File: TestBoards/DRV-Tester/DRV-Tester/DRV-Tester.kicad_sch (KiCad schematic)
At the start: 0 parts

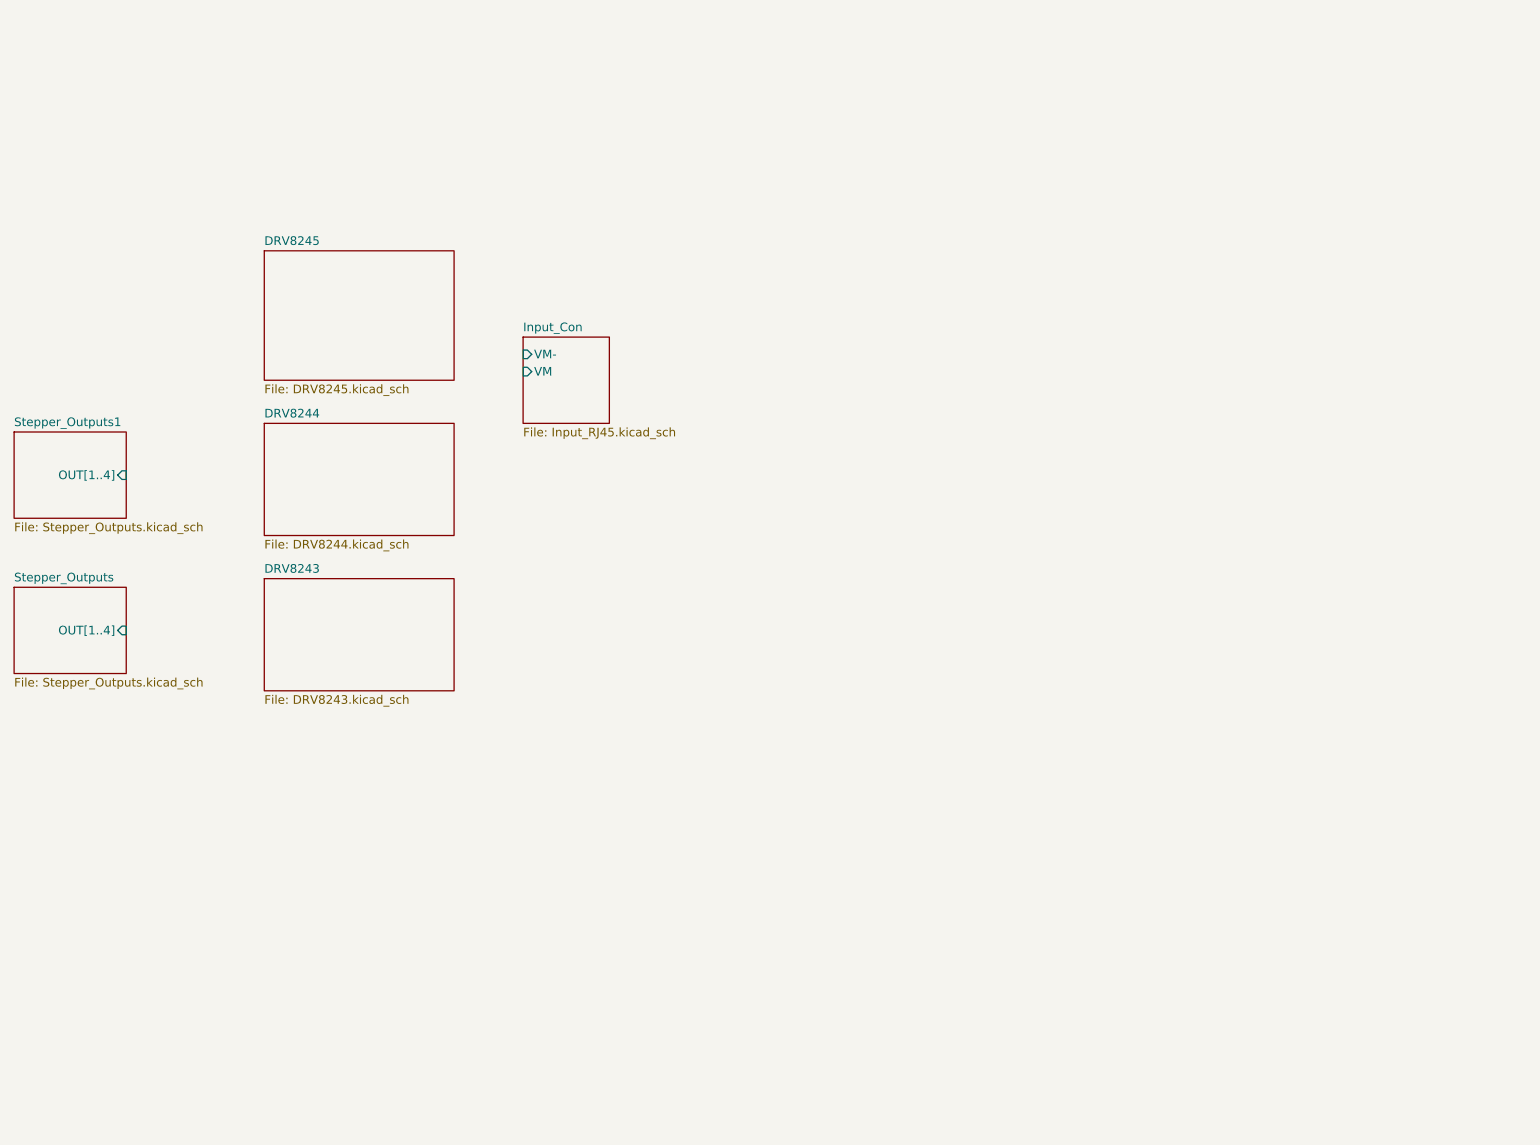
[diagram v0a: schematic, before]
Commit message: update new tester board sch
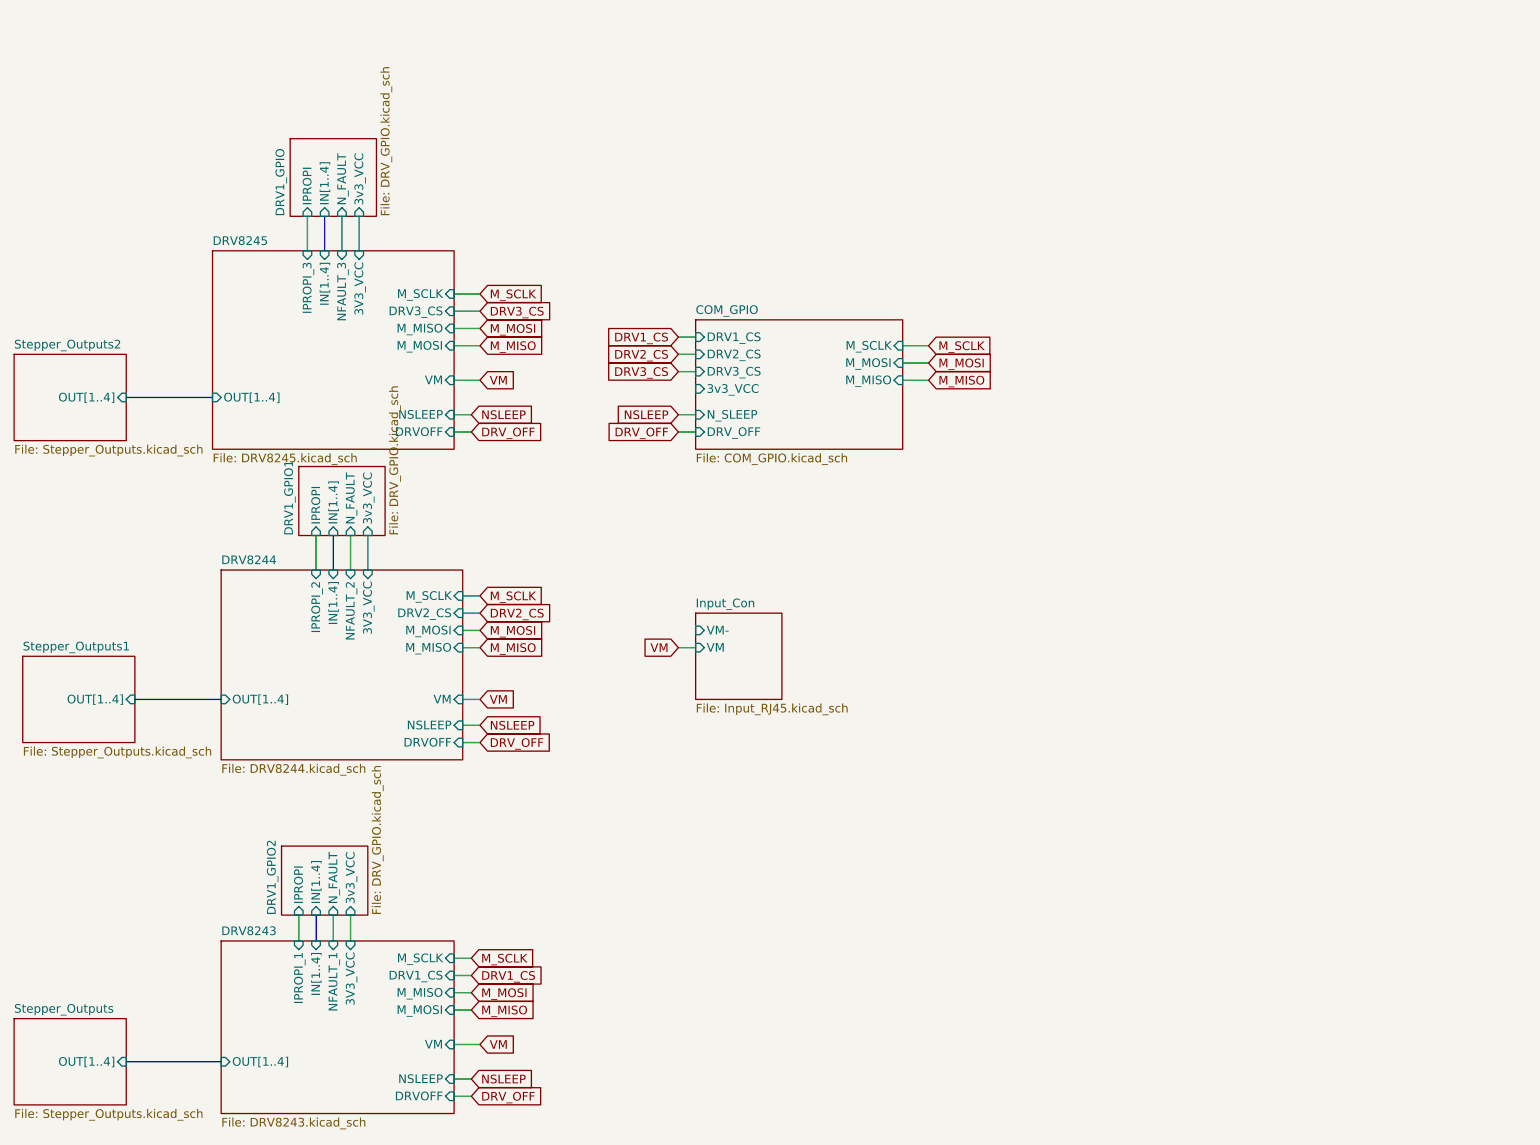
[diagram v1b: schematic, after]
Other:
- added sheet COM_GPIO (COM_GPIO.kicad_sch)
- added sheet DRV1_GPIO (DRV_GPIO.kicad_sch)
- added sheet DRV1_GPIO1 (DRV_GPIO.kicad_sch)
- added sheet DRV1_GPIO2 (DRV_GPIO.kicad_sch)
- added sheet Stepper_Outputs2 (Stepper_Outputs.kicad_sch)
- sheet DRV8243 ports: added 3V3_VCC, DRV1_CS, DRVOFF, IN[1..4], IPROPI_1, M_MISO, M_MOSI, M_SCLK, NFAULT_1, NSLEEP, OUT[1..4], VM; removed none
- sheet DRV8244 ports: added 3V3_VCC, DRV2_CS, DRVOFF, IN[1..4], IPROPI_2, M_MISO, M_MOSI, M_SCLK, NFAULT_2, NSLEEP, OUT[1..4], VM; removed none
- sheet DRV8245 ports: added 3V3_VCC, DRV3_CS, DRVOFF, IN[1..4], IPROPI_3, M_MISO, M_MOSI, M_SCLK, NFAULT_3, NSLEEP, OUT[1..4], VM; removed none

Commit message: update tester board with layout
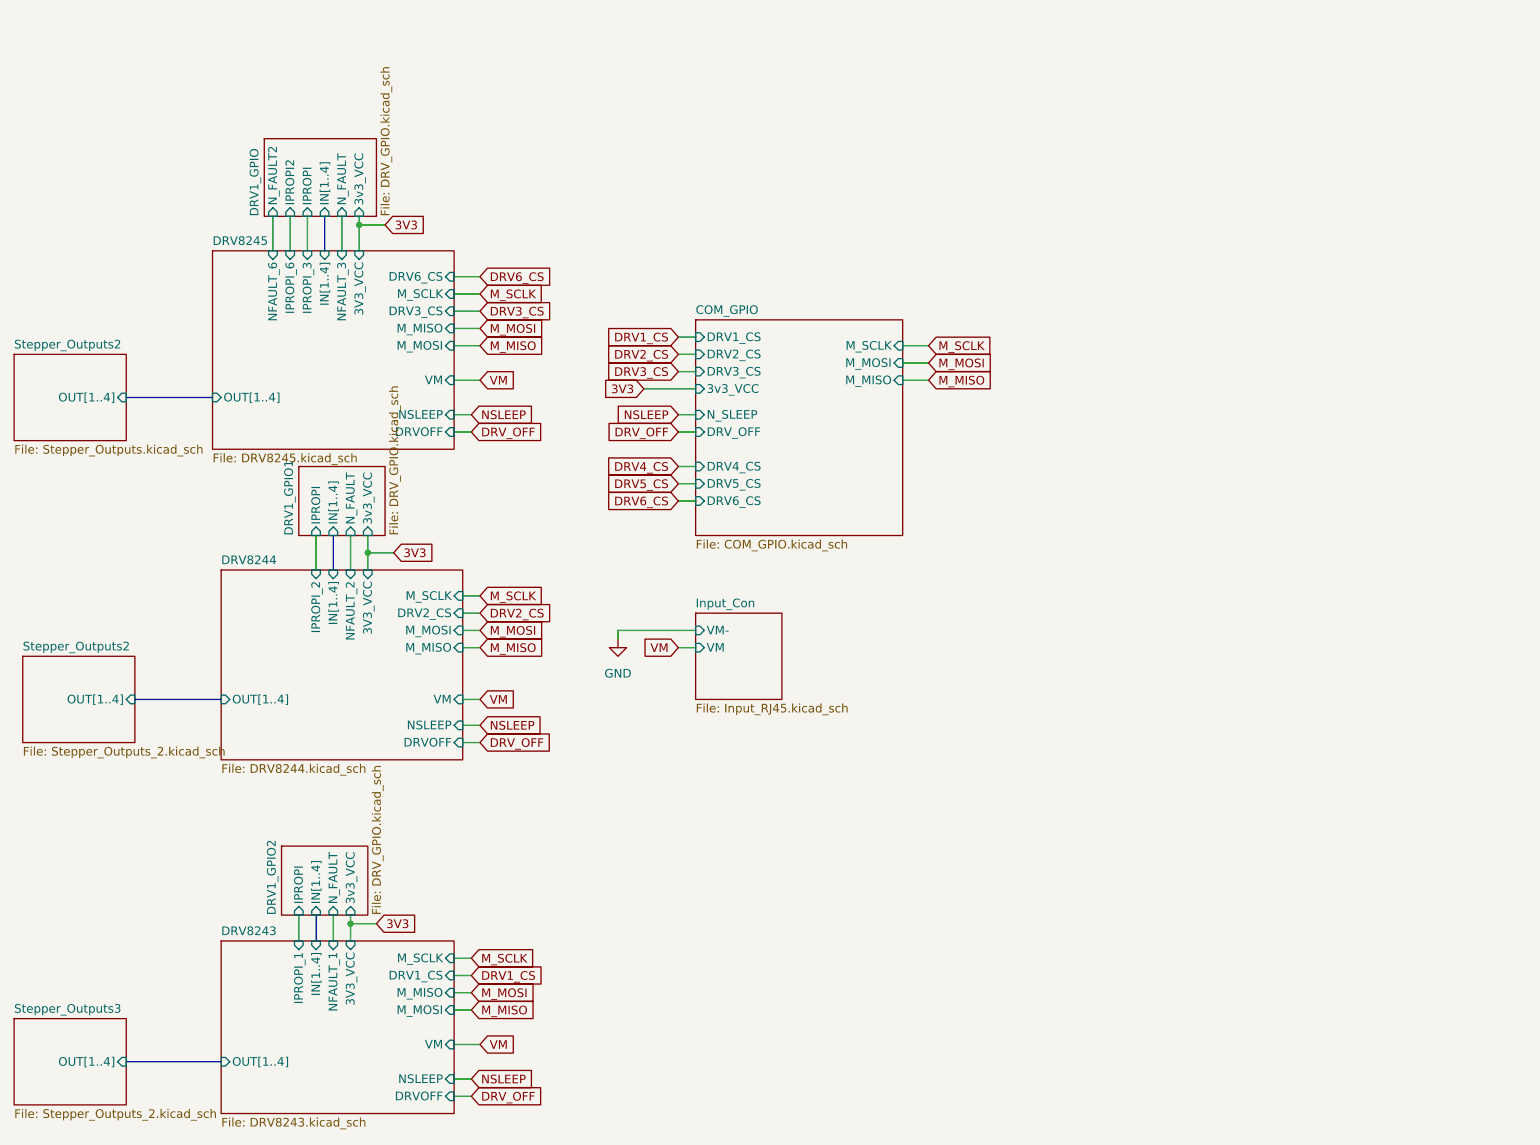
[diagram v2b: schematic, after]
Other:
- sheet Stepper_Outputs renamed Stepper_Outputs3
- removed sheet Stepper_Outputs1
- sheet COM_GPIO ports: added DRV4_CS, DRV5_CS, DRV6_CS; removed none
- sheet DRV1_GPIO ports: added IPROPI2, N_FAULT2; removed none
- sheet DRV8245 ports: added DRV6_CS, IPROPI_6, NFAULT_6; removed none
- sheet Stepper_Outputs3: file Stepper_Outputs.kicad_sch -> Stepper_Outputs_2.kicad_sch

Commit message: add caps and LEDs to testboard
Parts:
- added C1: 22uF, Capacitor_SMD:C_1210_3225Metric, symbol Device:C
- added C2, C4, C5: 10uF, Capacitor_SMD:C_1210_3225Metric, symbol Device:C
- added C3: 10uF, Capacitor_SMD:C_0603_1608Metric, symbol Device:C
- added C6, C7, C8, C9: EEU-FC1J101LB, SamacSys_Parts:CAPPRD350W65D800H1650, symbol SamacSys_Parts:EEU-FC1J101LB
- added R1: 500, Resistor_SMD:R_0603_1608Metric, symbol Device:R_US
- added R2: 8.2k, Resistor_SMD:R_0603_1608Metric, symbol Device:R_US
- added V3v1, VM1: LED, LED_SMD:LED_0603_1608Metric, symbol Device:LED
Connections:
- net 3V3: now also V3v1.2 (A)
- net GND: now also C1.2, C2.2, C3.2, C4.2, C5.2, C6.2 (-), C7.2 (-), C8.2 (-), C9.2 (-), R1.1, R2.1
- net VM: now also C1.1, C2.1, C3.1, C4.1, C5.1, C6.1 (+), C7.1 (+), C8.1 (+), C9.1 (+), VM1.2 (A)
- new net: R2.2, VM1.1 (K)
- new net: R1.2, V3v1.1 (K)
